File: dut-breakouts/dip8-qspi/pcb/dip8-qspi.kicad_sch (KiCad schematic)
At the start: 10 parts, among them J1 CONN_DUMPTRUCK_DEVICE, U1 M24C02-RMC6TG, U2 DUT_SOCKET

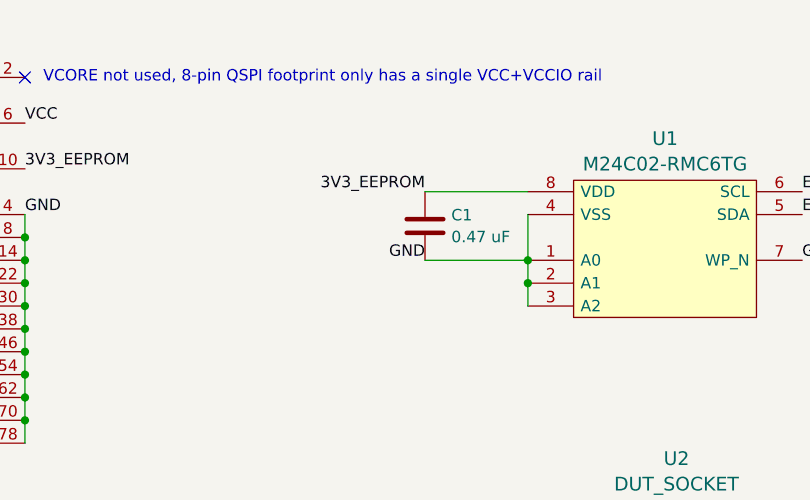
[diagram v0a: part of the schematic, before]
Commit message: dip8-qspi: changed eeprom address to 0xa2
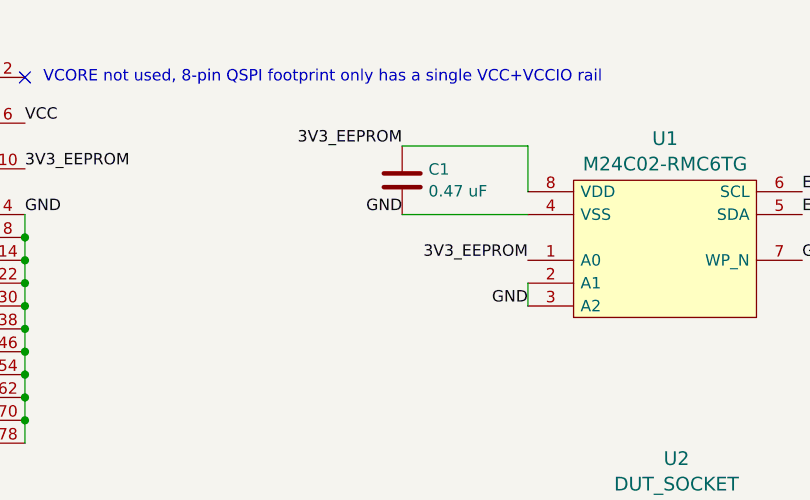
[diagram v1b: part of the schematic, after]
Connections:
- net 3V3_EEPROM: now also U1.1 (A0)
- net GND: no longer U1.1 (A0)
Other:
- moved on the sheet: C1
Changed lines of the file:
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@@
 	(generator_version "8.0")
 	(paper "A4")
+	(title_block
+		(date "2024-11-30")
+	)
 	(junction
 		(at 35.56 48.26)
@@
 	)
 	(junction
-		(at 124.46 45.72)
-		(diameter 0)
-		(color 0 0 0 0)
-	)
-	(junction
-		(at 124.46 43.18)
-		(diameter 0)
-		(color 0 0 0 0)
-	)
-	(junction
 		(at 68.58 48.26)
 		(diameter 0)
@@
 	(wire
 		(pts
+			(xy 124.46 30.48) (xy 124.46 35.56)
+		)
+		(stroke
+			(width 0)
+			(type default)
+		)
+	)
+	(wire
+		(pts
 			(xy 68.58 40.64) (xy 68.58 43.18)
 		)
@@
 	(wire
 		(pts
+			(xy 110.49 38.1) (xy 124.46 38.1)
+		)
+		(stroke
+			(width 0)
+			(type default)
+		)
+	)
+	(wire
+		(pts
 			(xy 68.58 60.96) (xy 68.58 63.5)
 		)
@@
 	(wire
 		(pts
+			(xy 110.49 30.48) (xy 124.46 30.48)
+		)
+		(stroke
+			(width 0)
+			(type default)
+		)
+	)
+	(wire
+		(pts
 			(xy 68.58 58.42) (xy 68.58 60.96)
 		)
@@
 	(wire
 		(pts
-			(xy 113.03 35.56) (xy 124.46 35.56)
-		)
-		(stroke
-			(width 0)
-			(type default)
-		)
-	)
-	(wire
-		(pts
-			(xy 113.03 43.18) (xy 124.46 43.18)
-		)
-		(stroke
-			(width 0)
-			(type default)
-		)
-	)
-	(wire
-		(pts
-			(xy 124.46 43.18) (xy 124.46 45.72)
-		)
-		(stroke
-			(width 0)
-			(type default)
-		)
-	)
-	(wire
-		(pts
 			(xy 35.56 58.42) (xy 35.56 60.96)
 		)
@@
 		(pts
 			(xy 35.56 48.26) (xy 35.56 50.8)
-		)
-		(stroke
-			(width 0)
-			(type default)
-		)
-	)
-	(wire
-		(pts
-			(xy 124.46 38.1) (xy 124.46 43.18)
 		)
 		(stroke
@@
 		)
 	)
+	(label "3V3_EEPROM"
+		(at 124.46 43.18 180)
+		(fields_autoplaced yes)
+		(effects
+			(font
+				(size 1.27 1.27)
+			)
+			(justify right bottom)
+		)
+	)
 	(label "QSPI_DQ3"
 		(at 160.02 74.93 0)
@@
 	)
 	(label "3V3_EEPROM"
-		(at 113.03 35.56 180)
+		(at 110.49 30.48 180)
 		(fields_autoplaced yes)
 		(effects
@@
 		)
 	)
+	(label "GND"
+		(at 124.46 48.26 180)
+		(fields_autoplaced yes)
+		(effects
+			(font
+				(size 1.27 1.27)
+			)
+			(justify right bottom)
+		)
+	)
 	(label "EEPROM_SDA"
 		(at 154.94 38.1 0)
@@
 	)
 	(label "GND"
-		(at 113.03 43.18 180)
+		(at 110.49 38.1 180)
 		(fields_autoplaced yes)
 		(effects
@@
 	(symbol
 		(lib_id "device:C")
-		(at 113.03 39.37 0)
+		(at 110.49 34.29 0)
 		(unit 1)
 		(exclude_from_sim no)
@@
 		(fields_autoplaced yes)
 		(property "Reference" "C1"
-			(at 115.951 38.1578 0)
+			(at 113.411 33.0778 0)
 			(effects
 				(font
@@
 		)
 		(property "Value" "0.47 uF"
-			(at 115.951 40.5821 0)
+			(at 113.411 35.5021 0)
 			(effects
 				(font
@@
 		)
 		(property "Footprint" "azonenberg_pcb:EIA_0402_CAP_NOSILK"
-			(at 113.9952 43.18 0)
+			(at 111.4552 38.1 0)
 			(effects
 				(font
@@
 		)
 		(property "Datasheet" ""
-			(at 113.03 39.37 0)
+			(at 110.49 34.29 0)
 			(effects
 				(font
@@
 		)
 		(property "Description" "Unpolarized capacitor"
-			(at 113.03 39.37 0)
-			(effects
-				(font
+			(at 110.49 34.29 0)
+			(effects
+				(font
